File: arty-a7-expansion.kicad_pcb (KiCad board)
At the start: 4 copper layers, 109.4 x 40 mm, 62 parts, among them IC1 TPD8S009DSMR, J2 1140084168, J4 685119134923, J5 UE27AC54100, U1 TPS61232DRCT, U2 MAX3421EEHJ, Y1 KX-7_12.MHz

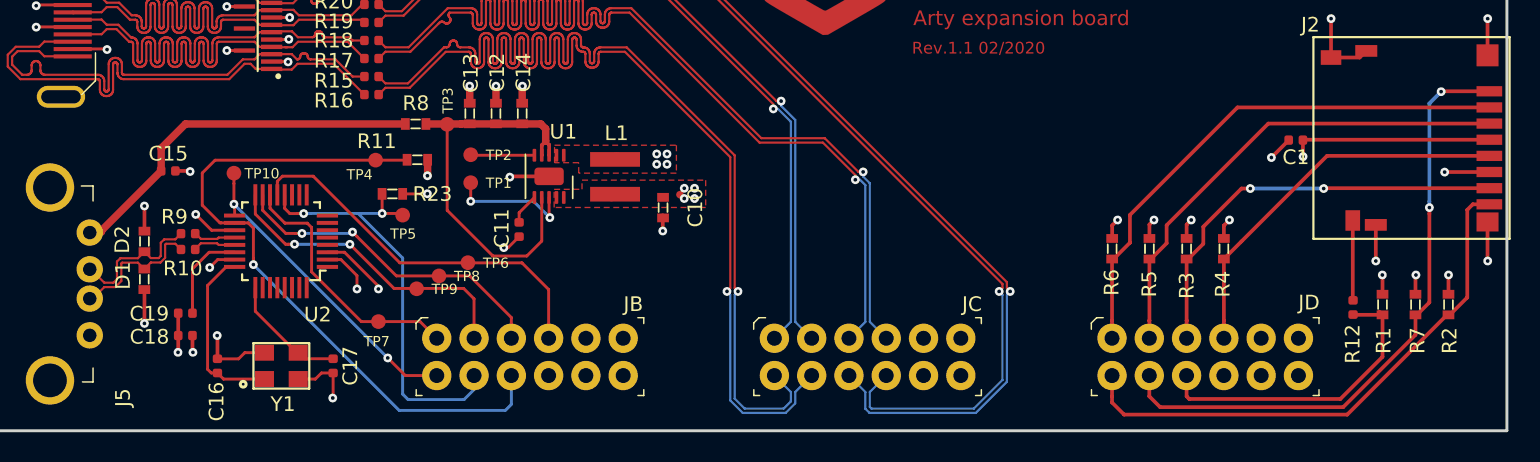
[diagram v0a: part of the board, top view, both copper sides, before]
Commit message: Standardize components
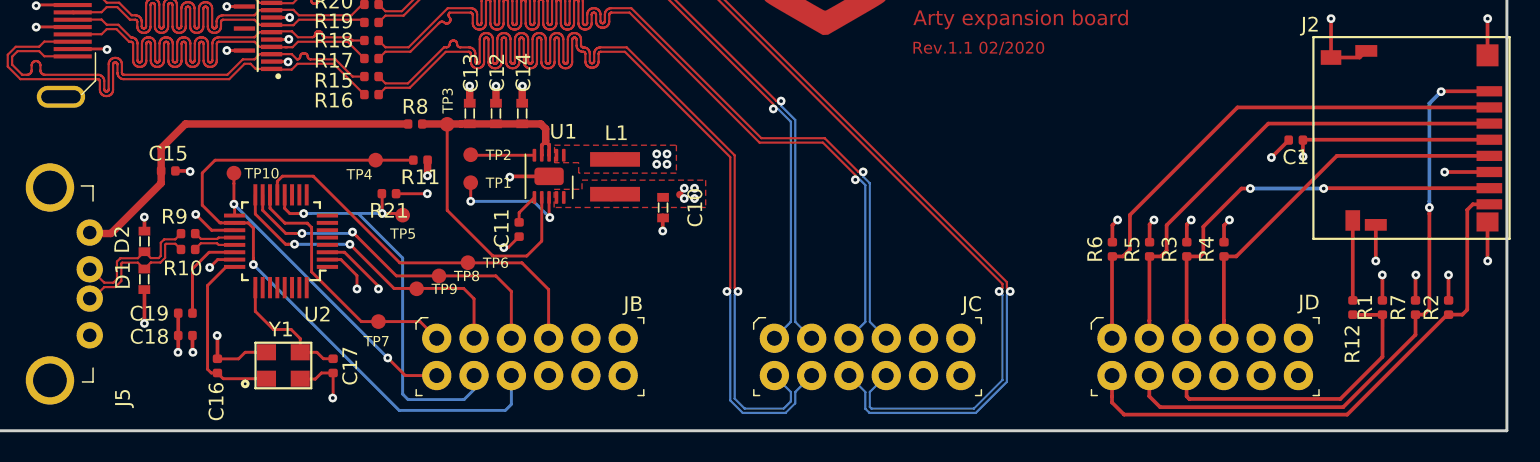
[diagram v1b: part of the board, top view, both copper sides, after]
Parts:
- removed R23: R_0R_0603, arty-a7-expansion-footprints:0603-res
- added R21: R_0R_0402, arty-a7-expansion-footprints:0402-res, F.Cu at (124.4, 108.3)
- R1, R2, R3, R4, R5, R6, R7: value R_20k_0603 -> R_20k_0402; footprint arty-a7-expansion-footprints:0603-res -> arty-a7-expansion-footprints:0402-res
- R11: value R_10k_0603 -> R_10k_0402; footprint arty-a7-expansion-footprints:0603-res -> arty-a7-expansion-footprints:0402-res
- R8: value R_0R_0603 -> R_0R_0402; footprint arty-a7-expansion-footprints:0603-res -> arty-a7-expansion-footprints:0402-res
- Y1: value KX-7_12.MHz -> ABM8G-12.000MHZ-18-D2Y-T
- moved R11 0.21 mm to (126.5, 106.0)
- moved R2 0.20 mm to (196.6, 116.1), turned to 90 degrees
- moved R1 0.20 mm to (192.1, 116.1), turned to 90 degrees
- moved R7 0.20 mm to (194.3, 116.1), turned to 90 degrees
- moved Y1 0.14 mm to (117.2, 120.0)
- turned R6 to 90 degrees
- turned R5 to 90 degrees
- turned R3 to 90 degrees
- turned R4 to 90 degrees
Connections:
- R1 pad 1: +3V3 -> /CD
- R1 pad 2: /CD -> +3V3
- R2 pad 1: +3V3 -> /DAT1
- R2 pad 2: /DAT1 -> +3V3
- R3 pad 1: +3V3 -> /MISO_DAT0
- R3 pad 2: /MISO_DAT0 -> +3V3
- R4 pad 1: +3V3 -> /SCK
- R4 pad 2: /SCK -> +3V3
- R5 pad 1: +3V3 -> /MOSI_CMD
- R5 pad 2: /MOSI_CMD -> +3V3
- R6 pad 1: +3V3 -> /CD_DAT3
- R6 pad 2: /CD_DAT3 -> +3V3
- R7 pad 1: +3V3 -> /DAT2
- R7 pad 2: /DAT2 -> +3V3
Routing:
- net +3V3: track 35.5 -> 38.4 mm
- net /MISO_USB: track 22.5 -> 23.6 mm
- net GND: track 68.0 -> 67.3 mm
- net +5V: track 25.5 -> 26.0 mm
- net /XO: track 8.25 -> 8.80 mm
- net /DAT1: track 37.3 -> 37.8 mm

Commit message: Update mpn
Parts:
- moved C16 0.95 mm to (113.7, 120.0)
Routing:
- net GND: track 67.3 -> 65.1 mm

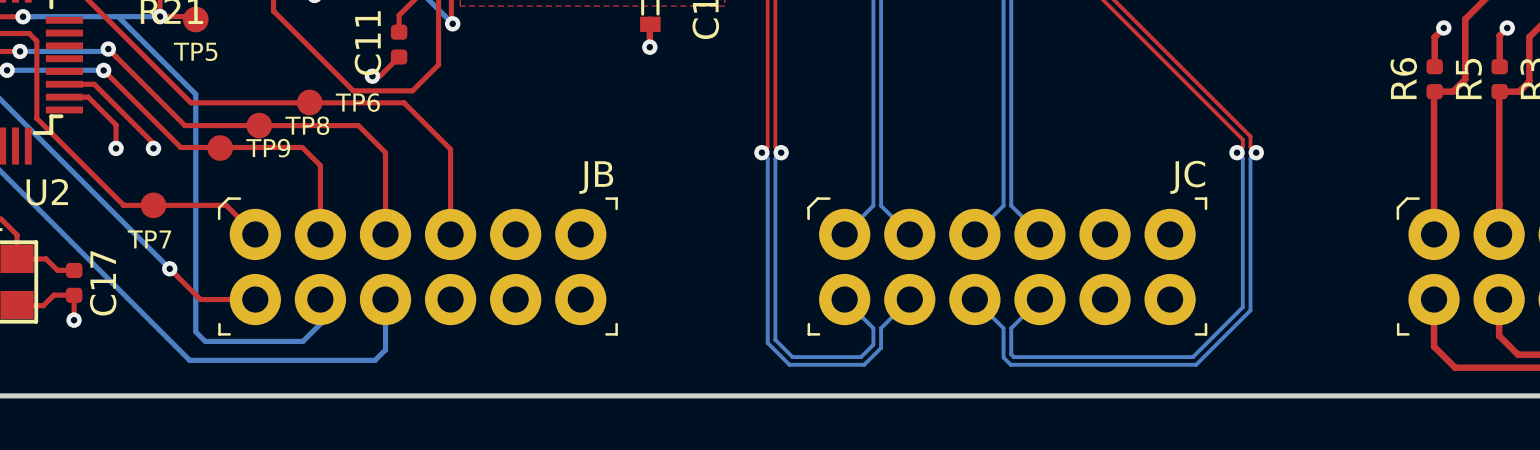
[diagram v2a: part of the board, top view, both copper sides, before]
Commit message: Update library references
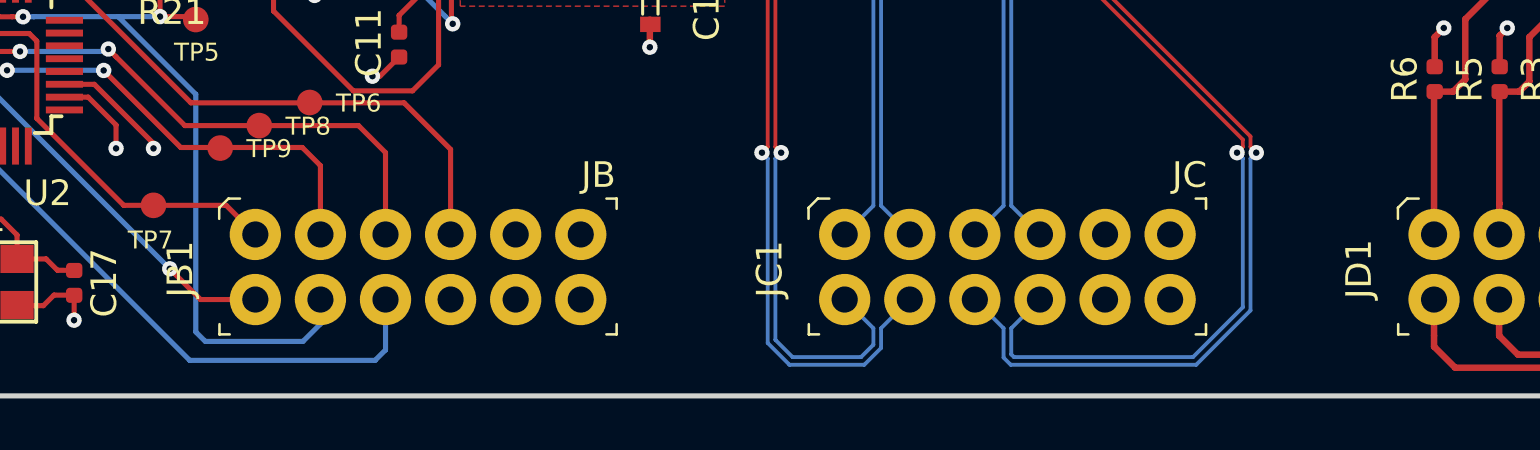
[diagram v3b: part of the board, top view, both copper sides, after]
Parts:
- JB1, JC1, JD1: footprint HDMI_SD_expansion-footprints:PinHeader_6x2_P2.54mm_Horizontal_Mirrored -> arty-a7-expansion-footprints:PinHeader_6x2_P2.54mm_Horizontal_Mirrored
- N1: footprint HDMI_SD_expansion-footprints:antmicro-logo_scaled_30mm -> arty-a7-expansion-footprints:antmicro-logo_scaled_30mm

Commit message: Add revision 2.0.1
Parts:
- added C2: C_100n_0402_16V, arty-a7-expansion-footprints:0402-cap, F.Cu at (177.0, 81.9)
- added C20: C_10u_0402, arty-a7-expansion-footprints:0402-cap, F.Cu at (186.6, 67.9)
- added C21: C_100n_0402_16V, arty-a7-expansion-footprints:0402-cap, F.Cu at (186.9, 80.3)
- added C22: C_100n_0402_16V, arty-a7-expansion-footprints:0402-cap, F.Cu at (178.8, 68.4)
- added C23: C_10u_0402, arty-a7-expansion-footprints:0402-cap, F.Cu at (185.9, 80.3)
- added C24: C_1u_0402, arty-a7-expansion-footprints:0402-cap, F.Cu at (178.8, 67.4)
- added C25: C_3u3_0603, arty-a7-expansion-footprints:0603-cap, F.Cu at (187.1, 84.7)
- added C26: C_3u3_0603, arty-a7-expansion-footprints:0603-cap, F.Cu at (187.1, 76.8)
- added C27: C_1u_0402, arty-a7-expansion-footprints:0402-cap, F.Cu at (186.0, 72.1)
- added C28: C_1u_0402, arty-a7-expansion-footprints:0402-cap, F.Cu at (187.4, 65.6)
- added C29: C_2n7_0603, arty-a7-expansion-footprints:0603-cap, F.Cu at (190.9, 84.4)
- added C3: C_100n_0402_16V, arty-a7-expansion-footprints:0402-cap, F.Cu at (178.2, 72.5)
- added C30: C_2n7_0603, arty-a7-expansion-footprints:0603-cap, F.Cu at (190.9, 77.0)
- added C31: C_100n_0402_6V3, arty-a7-expansion-footprints:0402-cap, F.Cu at (169.3, 69.0)
- added C32: C_180p_0402, arty-a7-expansion-footprints:0402-cap, F.Cu at (184.6, 66.4)
- added C33: C_180p_0402, arty-a7-expansion-footprints:0402-cap, F.Cu at (186.0, 71.0)
- added C4: C_4u7_0402, arty-a7-expansion-footprints:0402-cap, F.Cu at (179.0, 81.9)
- added C5: C_4u7_0402, arty-a7-expansion-footprints:0402-cap, F.Cu at (178.8, 70.9)
- added C6: C_100n_0402_16V, arty-a7-expansion-footprints:0402-cap, F.Cu at (178.0, 81.9)
- added C7: C_100n_0402_16V, arty-a7-expansion-footprints:0402-cap, F.Cu at (178.8, 69.9)
- added C8: C_100n_0402_16V, arty-a7-expansion-footprints:0402-cap, F.Cu at (183.1, 78.1)
- added C9: C_10u_0402, arty-a7-expansion-footprints:0402-cap, F.Cu at (179.8, 78.8)
- added D3: LG_L29K-G2J1-24-Z, arty-a7-expansion-footprints:LED_0603, F.Cu at (161.4, 66.6)
- added D4: LG_L29K-G2J1-24-Z, arty-a7-expansion-footprints:LED_0603, F.Cu at (159.6, 66.6)
- added D5: LG_L29K-G2J1-24-Z, arty-a7-expansion-footprints:LED_0603, F.Cu at (157.9, 66.6)
- added D6: LG_L29K-G2J1-24-Z, arty-a7-expansion-footprints:LED_0603, F.Cu at (156.1, 66.6)
- added FB1: BLM15AG601SN1D, arty-a7-expansion-footprints:0402-res, F.Cu at (177.5, 80.3)
- added FB2: BLM15AG601SN1D, arty-a7-expansion-footprints:0402-res, F.Cu at (179.3, 72.5)
- added IC2: PCA9500PW, arty-a7-expansion-footprints:TSSOP-16, F.Cu at (166.5, 72.7)
- added J1: SJ-43516-SMT-GR, arty-a7-expansion-footprints:CUI_SJ-43516-SMT-GR, F.Cu at (199.9, 80.1)
- added J3: SJ-43516-SMT-BE, arty-a7-expansion-footprints:CUI_SJ-43516-SMT-BE, F.Cu at (199.9, 68.4)
- added JA1: 10883121, arty-a7-expansion-footprints:PinHeader_6x2_P2.54mm_Horizontal_Mirrored, F.Cu at (114.2, 102.7)
- added R22: R_1R_0402, arty-a7-expansion-footprints:0402-res, F.Cu at (178.5, 83.4)
- added R23: R_1R_0402, arty-a7-expansion-footprints:0402-res, F.Cu at (177.2, 70.4)
- added R24: R_10k_0402, arty-a7-expansion-footprints:0402-res, F.Cu at (183.1, 73.0)
- added R25: R_0R_0402, arty-a7-expansion-footprints:0402-res, F.Cu at (181.0, 73.0)
- added R26: R_0R_0402, arty-a7-expansion-footprints:0402-res, F.Cu at (181.5, 72.5)
- added R27: R_0R_0402, arty-a7-expansion-footprints:0402-res, F.Cu at (178.8, 74.5)
- added R28: R_10k_0402, arty-a7-expansion-footprints:0402-res, F.Cu at (189.4, 86.2)
- added R29: R_5k1_0603, arty-a7-expansion-footprints:0603-res, F.Cu at (186.0, 73.4)
- added R30: R_10k_0402, arty-a7-expansion-footprints:0402-res, F.Cu at (189.4, 75.3)
- added R31: R_5k1_0603, arty-a7-expansion-footprints:0603-res, F.Cu at (187.4, 64.3)
- added R32: R_470R_0402, arty-a7-expansion-footprints:0402-res, F.Cu at (189.4, 84.1)
- added R33: R_470R_0402, arty-a7-expansion-footprints:0402-res, F.Cu at (189.4, 77.3)
- added R34: R_5k1_0603, arty-a7-expansion-footprints:0603-res, F.Cu at (188.7, 73.4)
- added R35: R_5k1_0603, arty-a7-expansion-footprints:0603-res, F.Cu at (190.2, 64.3)
- added R36: R_2k_0402, arty-a7-expansion-footprints:0402-res, F.Cu at (171.7, 70.5)
- added R37: R_2k_0402, arty-a7-expansion-footprints:0402-res, F.Cu at (171.7, 72.4)
- added R38: R_100k_0402, arty-a7-expansion-footprints:0402-res, F.Cu at (166.8, 76.9)
- added R39: R_0R_0402, arty-a7-expansion-footprints:0402-res, F.Cu at (166.3, 76.5)
- added R40: R_100R_0402, arty-a7-expansion-footprints:0402-res, F.Cu at (161.4, 64.0)
- added R41: R_100R_0402, arty-a7-expansion-footprints:0402-res, F.Cu at (159.6, 64.0)
- added R42: R_100R_0402, arty-a7-expansion-footprints:0402-res, F.Cu at (157.9, 64.0)
- added R43: R_100R_0402, arty-a7-expansion-footprints:0402-res, F.Cu at (156.1, 64.0)
- added U3: CS4344-CZZ, arty-a7-expansion-footprints:10TSSOP, F.Cu at (182.3, 80.8)
- added U4: CS5343-CZZ, arty-a7-expansion-footprints:10TSSOP, F.Cu at (182.6, 68.9)
- added U5: NC7SZ126P5X, arty-a7-expansion-footprints:SC-70-5, F.Cu at (182.9, 75.2)
- JB1, JC1, JD1: value 0015912120 -> 10883121
- L1: value XFL4020-102MEB -> XFL4020-102MEC
- moved C16 26.1 mm to (122.5, 95.4)
- moved Y1 26.1 mm to (126.0, 95.4)
- moved C17 26.1 mm to (129.4, 95.5)
- moved N2 26.0 mm to (170.6, 84.1)
- moved L1 25.0 mm to (149.5, 84.1), turned to 90 degrees
- moved C10 24.8 mm to (152.1, 86.2)
- moved D1 24.8 mm to (116.8, 91.1)
- moved R11 24.8 mm to (135.6, 83.0)
- moved C11 24.8 mm to (142.3, 87.7)
- moved C14 24.8 mm to (142.5, 79.8)
- moved C15 24.8 mm to (118.4, 83.7)
- moved C19 24.8 mm to (119.6, 94.9)
- moved D2 24.8 mm to (116.8, 88.5)
- moved TP1 24.8 mm to (139.0, 84.4)
- moved TP10 24.8 mm to (122.9, 83.8)
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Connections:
- JB1 pad 10: Net-(JB1-Pad10) -> /GPIO_SCL
- JD1 pad 10: /NC_EN -> /GPIO_SDA
- L1 pad 1: Net-(L1-Pad1) -> +3V3
- L1 pad 2: +3V3 -> Net-(L1-Pad2)
- U1 pad 1: Net-(L1-Pad1) -> Net-(L1-Pad2)
- U1 pad 2: Net-(L1-Pad1) -> Net-(L1-Pad2)
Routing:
- net /ADIN_MCLK: track 0.00 -> 105.2 mm, vias 0 -> 2
- net /ADIN_LRCK: track 0.00 -> 103.0 mm, vias 0 -> 2
- net /ADIN_SCLK: track 0.00 -> 100.3 mm, vias 0 -> 2
- net /ADOUT_MCLK: track 0.00 -> 91.5 mm, vias 0 -> 2
- net /ADIN_SDOUT: track 0.00 -> 89.3 mm, vias 0 -> 2
- net /ADOUT_LRCK: track 0.00 -> 88.3 mm, vias 0 -> 2
- net /ADOUT_SCLK: track 0.00 -> 82.7 mm, vias 0 -> 2
- net /ADOUT_SDIN: track 0.00 -> 80.0 mm, vias 0 -> 2
- net /GPIO_SCL: track 0.00 -> 76.0 mm, vias 0 -> 1
- net /GPIO_SDA: track 0.00 -> 52.0 mm, vias 0 -> 1
- net GND: track 65.1 -> 104.3 mm, vias 29 -> 49
- net +3V3: track 38.5 -> 62.6 mm, vias 19 -> 27
- net Net-(J3-Pad3): track 0.00 -> 13.5 mm
- net Net-(C29-Pad1): track 0.00 -> 13.0 mm
- net Net-(D6-Pad2): track 0.00 -> 11.3 mm
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- added copper zone on F.Cu, net Net-(L1-Pad2)
- removed copper zone on F.Cu, net Net-(L1-Pad1)
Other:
- board size 109.4 x 40 mm -> 109.2 x 47 mm
- board text added: "Rev.2.0.1 07/2020"
- board text removed: "JB"
- board text removed: "JC"
- board text removed: "JD"
- board text removed: "Rev.1.1 02/2020"
